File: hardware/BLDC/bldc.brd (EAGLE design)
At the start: 51 x 40 mm, 78 parts, among them J1 PWR_2_XT30PW-M, J2 LINEAR_3_JST_PH_RA, J3 LINEAR_8_JST_PH_RA, U1 MA702, U10 MCP2542FD, U11 LDFM33PUR, U2 DRV8323RS, U3 TPN7R006PL, U4 TPN7R006PL, U5 TPN7R006PL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

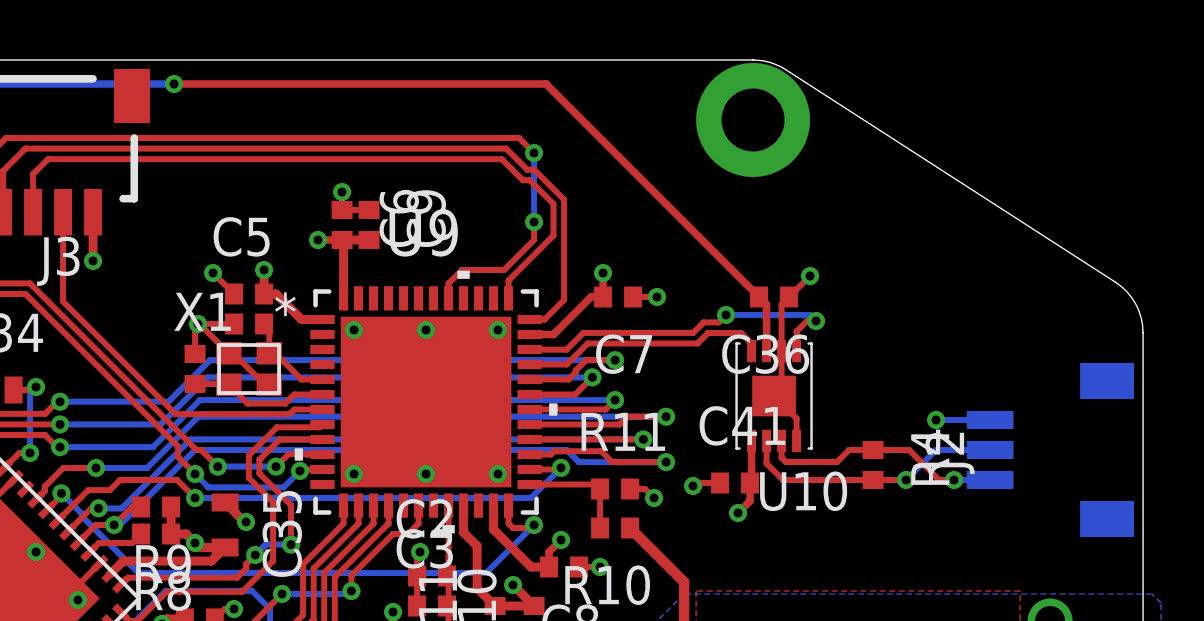
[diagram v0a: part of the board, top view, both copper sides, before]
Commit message: Added status LEDs
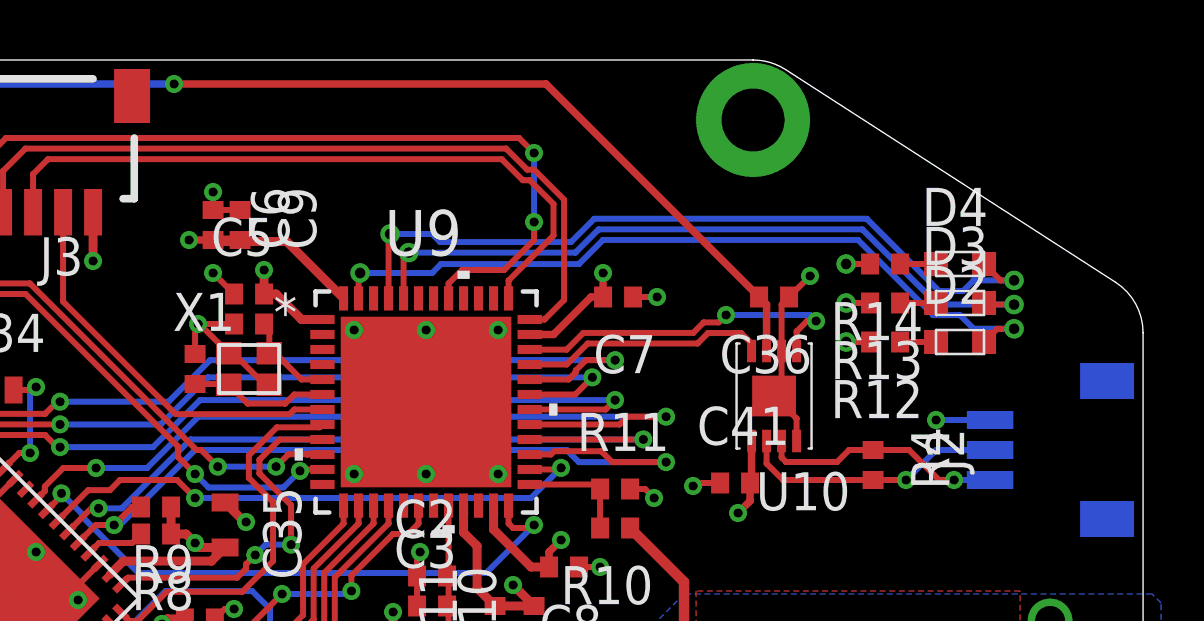
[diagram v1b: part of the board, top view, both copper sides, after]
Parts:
- added D2: 150060GS75000, _T_rcl:D0603
- added D3: 150060RS75000, _T_rcl:D0603
- added D4: 150060BS75000, _T_rcl:D0603
- added R12, R14: 5, _T_rcl:R0402
- added R13: 65, _T_rcl:R0402
- moved C6 4.30 mm to (20.0, 34.5)
- moved C9 4.30 mm to (20.9, 34.5)
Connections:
- new net N$10: D2.1, R12.2
- new net N$4: D4.1, R14.2
- new net N$7: D3.1, R13.2
- net GND: now also R12.1, R13.1, R14.1
- net LED1: now also D2.2
- net LED2: now also D3.2
- net LED3: now also D4.2
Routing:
- net LED3: track 0.00 -> 25.8 mm, vias 0 -> 2
- net LED1: track 0.00 -> 25.5 mm, vias 0 -> 2
- net LED2: track 0.00 -> 24.2 mm, vias 0 -> 2
- net +3V3: track 40.1 -> 43.3 mm
- net GND: track 58.4 -> 60.8 mm, vias 121 -> 124
- net N$7: track 0.00 -> 1.20 mm
- net N$4: track 0.00 -> 1.20 mm
- net N$10: track 0.00 -> 1.20 mm

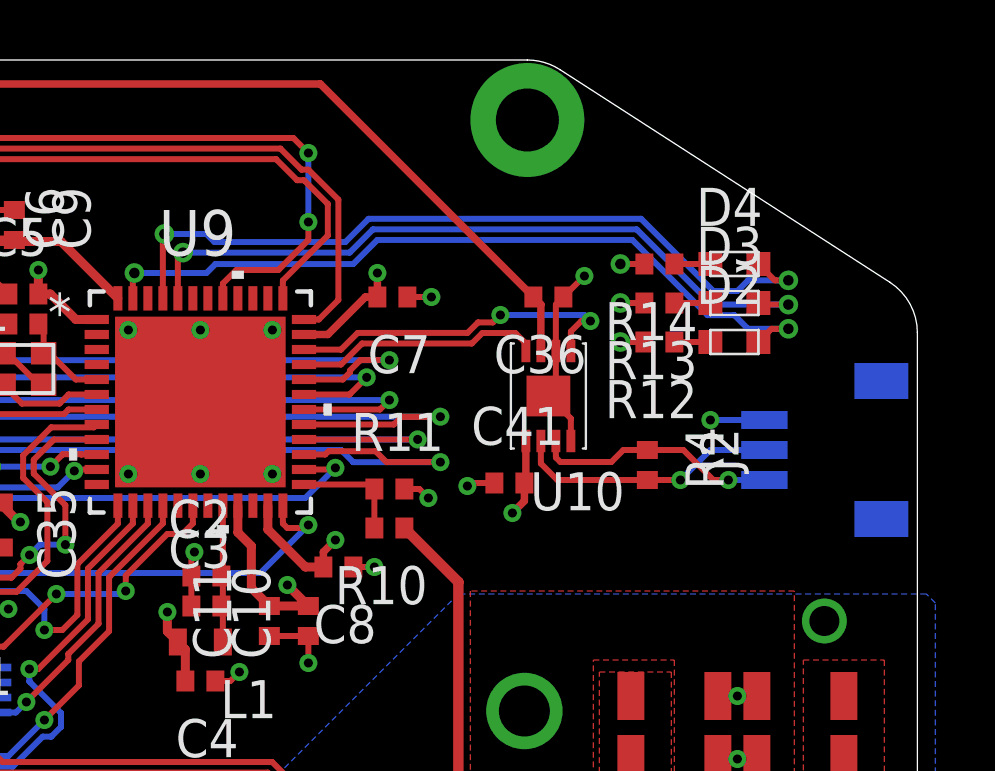
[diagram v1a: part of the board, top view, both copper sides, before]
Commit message: Moved LEDs
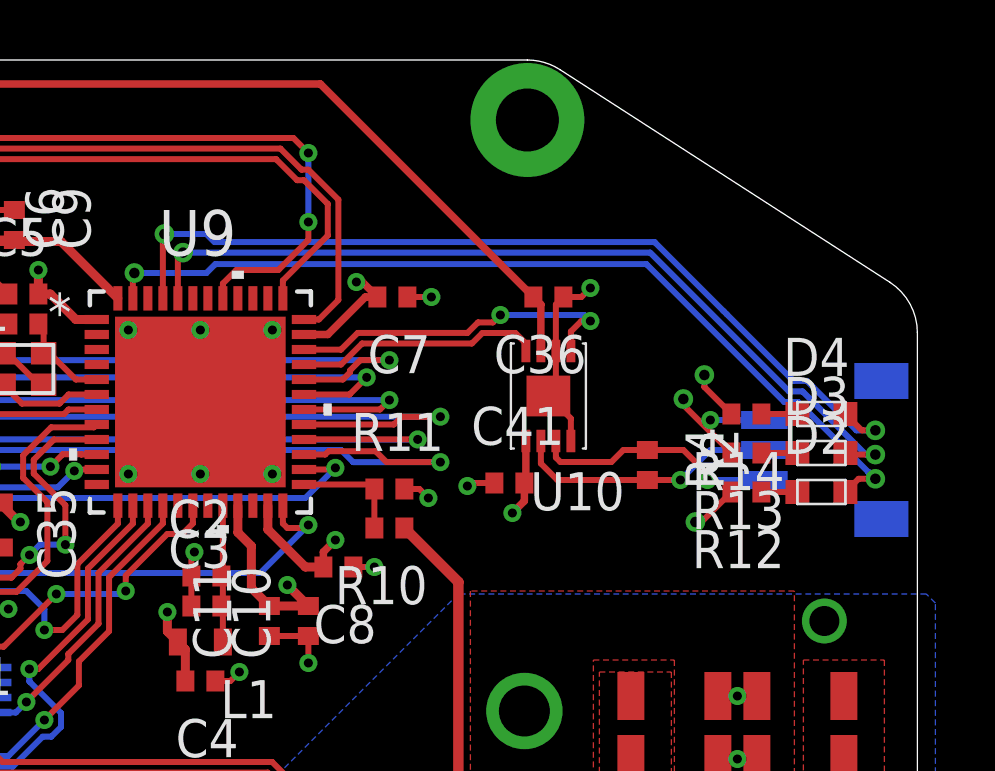
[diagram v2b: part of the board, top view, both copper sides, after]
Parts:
- moved D4 5.78 mm to (47.8, 28.2)
- moved R14 5.78 mm to (45.3, 28.2)
- moved D2 5.78 mm to (47.8, 25.6)
- moved D3 5.78 mm to (47.8, 26.9)
- moved R12 5.78 mm to (45.3, 25.6)
- moved R13 5.78 mm to (45.3, 26.9)
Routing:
- net LED2: track 24.2 -> 28.5 mm
- net LED1: track 25.5 -> 29.8 mm
- net LED3: track 25.8 -> 29.8 mm
- net GND: track 60.8 -> 64.1 mm

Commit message: Prerotate
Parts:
- moved C1 2.33 mm to (20.7, 19.4), turned to 270 degrees
- moved U1 1.41 mm to (20.0, 20.0)
- moved C10 1.03 mm to (31.6, 20.8)
- moved C4 1.00 mm to (27.1, 18.3)
- moved R9 0.71 mm to (17.6, 25.6)
- moved C9 0.70 mm to (21.6, 34.5)
- moved R10 0.63 mm to (34.0, 24.2)
- moved L1 0.60 mm to (27.1, 20.0)
- moved C8 0.58 mm to (32.2, 22.8)
- moved C11 0.51 mm to (29.5, 20.8)
- moved C25 0.41 mm to (7.00, 10.0)
- moved C28 0.41 mm to (5.20, 10.0)
- moved C27 0.41 mm to (3.40, 10.0)
- moved U3 0.41 mm to (6.10, 5.72)
- moved C3 0.30 mm to (27.3, 21.5)
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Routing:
- net +3V3: track 43.4 -> 58.6 mm
- net SHA: track 14.2 -> 25.6 mm, vias 28 -> 30
- net ENC_SCK: track 13.7 -> 10.5 mm
- net GND: track 64.1 -> 66.7 mm, vias 124 -> 123
- net ENC_CS: track 12.1 -> 10.3 mm
- net ENC_MISO: track 14.5 -> 12.8 mm
- net ENC_MOSI: track 9.22 -> 7.80 mm
- net +24V: track 40.2 -> 39.5 mm
- net N$1: track 4.66 -> 5.26 mm

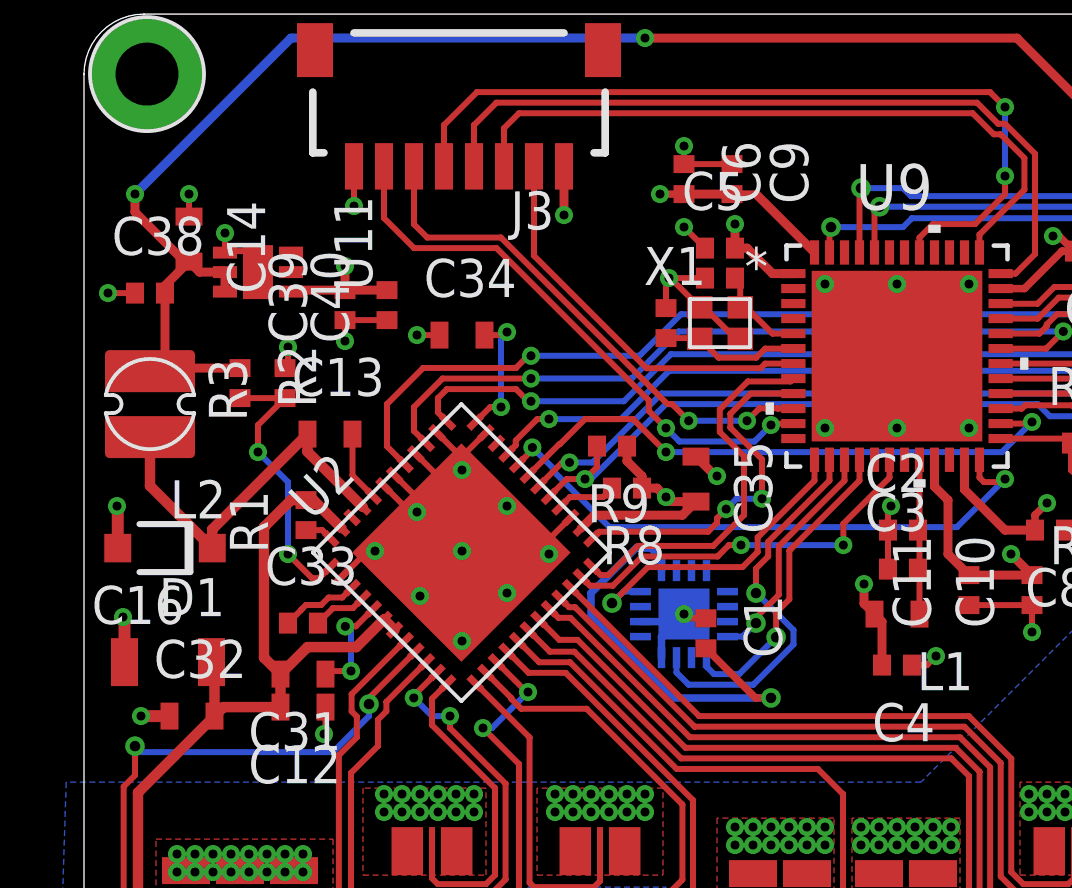
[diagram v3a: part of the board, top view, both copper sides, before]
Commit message: Fixed offset encoder
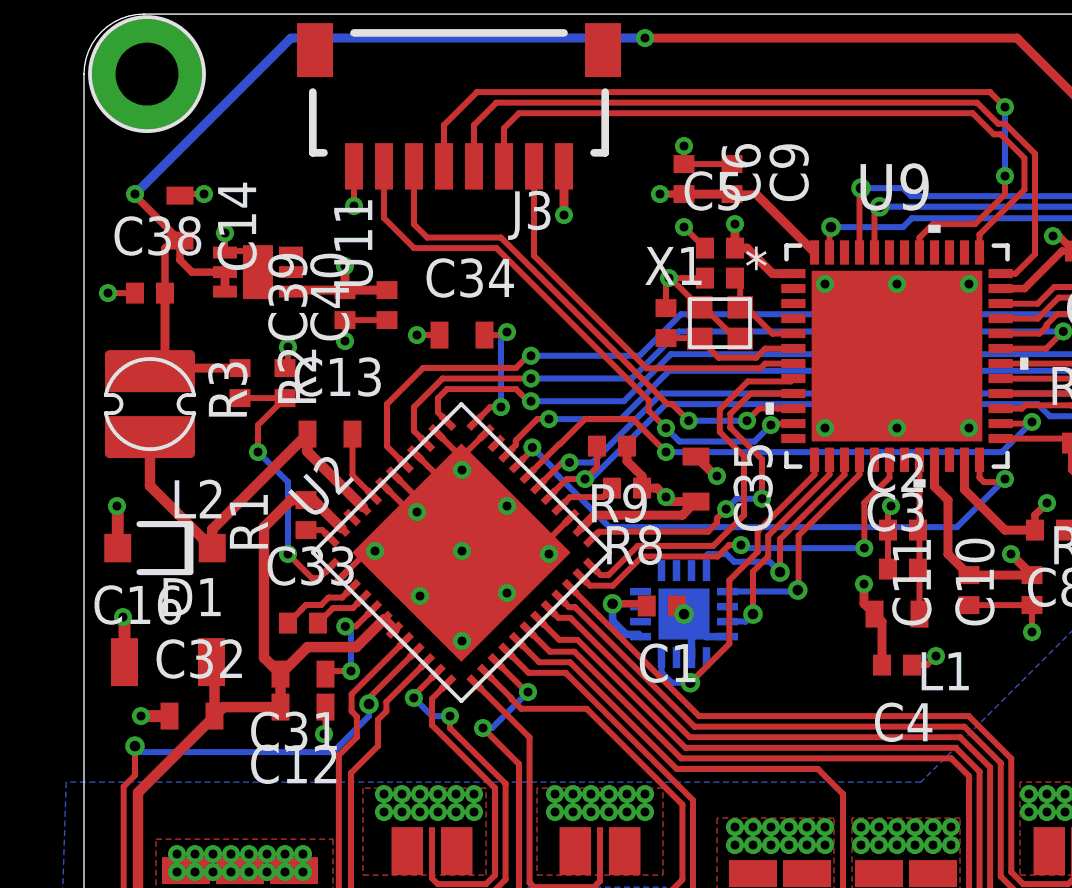
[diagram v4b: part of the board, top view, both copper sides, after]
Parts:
- moved C1 1.73 mm to (19.3, 20.3), turned to 180 degrees
- moved C14 0.76 mm to (3.20, 33.2)
- turned U1 to 270 degrees
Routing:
- net +3V3: track 58.6 -> 47.2 mm
- net ENC_MISO: track 12.8 -> 7.16 mm
- net ENC_CS: track 10.3 -> 7.56 mm
- net +5V: track 55.9 -> 56.7 mm
- net SENSE_C: track 12.9 -> 13.5 mm

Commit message: Prior to BOM consolidation
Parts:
- moved H1 0.10 mm to (2.00, 2.00)
- moved H2 0.10 mm to (2.00, 38.0)
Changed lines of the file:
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@@
 <layer number="1" name="Top" color="4" fill="1" visible="yes" active="yes"/>
 <layer number="2" name="Route2" color="16" fill="1" visible="yes" active="yes"/>
-<layer number="15" name="Route15" color="23" fill="1" visible="no" active="yes"/>
+<layer number="15" name="Route15" color="23" fill="1" visible="yes" active="yes"/>
 <layer number="16" name="Bottom" color="1" fill="1" visible="yes" active="yes"/>
 <layer number="17" name="Pads" color="2" fill="1" visible="yes" active="yes"/>
@@
 </layers>
 <board>
-<fusionsync huburn="a.YnVzaW5lc3M6Z21haWwyMjE5MTc" projecturn="a.YnVzaW5lc3M6Z21haWwyMjE5MTcjMjAxOTA2MjkyMDE0MTU5NzY" f3durn="urn:adsk.wipprod:dm.lineage:e4urj2y-ReajaBtUk_DaUw" pcbguid="" lastpulledtime="" lastsyncedchangeguid="" latestrevisionid="c8898aa8-4816-4024-a727-549153469479" lastsyncedrevisionid="c8898aa8-4816-4024-a727-549153469479" lastboardhashguid="96ba5604-6864-0f3b-cda7-083015d9c990" lastpushedtime="2020-05-19T04:17:52Z" linktopcb3d="%12"/>
+<fusionsync huburn="a.YnVzaW5lc3M6Z21haWwyMjE5MTc" projecturn="a.YnVzaW5lc3M6Z21haWwyMjE5MTcjMjAxOTA2MjkyMDE0MTU5NzY" f3durn="urn:adsk.wipprod:dm.lineage:e4urj2y-ReajaBtUk_DaUw" pcbguid="" lastpulledtime="" lastsyncedchangeguid="" latestrevisionid="0cfa6979-0abf-47e5-904f-7e41c382e9f9" lastsyncedrevisionid="0cfa6979-0abf-47e5-904f-7e41c382e9f9" lastboardhashguid="129d7aed-9189-2586-7fe0-9e496c46e9fb" lastpushedtime="2020-05-19T04:37:09Z" linktopcb3d="%12"/>
 <plain>
 <wire x1="39.0836" y1="39.681" x2="38" y2="40" width="0" layer="20" curve="32.8049"/>
@@
 <attribute name="VALUE" x="36.65" y="8.95" size="1.27" layer="27" rot="R180"/>
 </element>
-<element name="H1" library="_T_conn" library_urn="urn:adsk.eagle:library:19570503" package="M2" package3d_urn="urn:adsk.eagle:package:20293119/4" value="PCB_MOUNT_HOLE_M2" x="2.1" y="2" smashed="yes"/>
-<element name="H2" library="_T_conn" library_urn="urn:adsk.eagle:library:19570503" package="M2" package3d_urn="urn:adsk.eagle:package:20293119/4" value="PCB_MOUNT_HOLE_M2" x="2.1" y="38" smashed="yes"/>
+<element name="H1" library="_T_conn" library_urn="urn:adsk.eagle:library:19570503" package="M2" package3d_urn="urn:adsk.eagle:package:20293119/4" value="PCB_MOUNT_HOLE_M2" x="2" y="2" smashed="yes"/>
+<element name="H2" library="_T_conn" library_urn="urn:adsk.eagle:library:19570503" package="M2" package3d_urn="urn:adsk.eagle:package:20293119/4" value="PCB_MOUNT_HOLE_M2" x="2" y="38" smashed="yes"/>
 <element name="H3" library="_T_conn" library_urn="urn:adsk.eagle:library:19570503" package="M2" package3d_urn="urn:adsk.eagle:package:20293119/4" value="PCB_MOUNT_HOLE_M2" x="38" y="2" smashed="yes"/>
 <element name="H4" library="_T_conn" library_urn="urn:adsk.eagle:library:19570503" package="M2" package3d_urn="urn:adsk.eagle:package:20293119/4" value="PCB_MOUNT_HOLE_M2" x="38" y="38" smashed="yes"/>

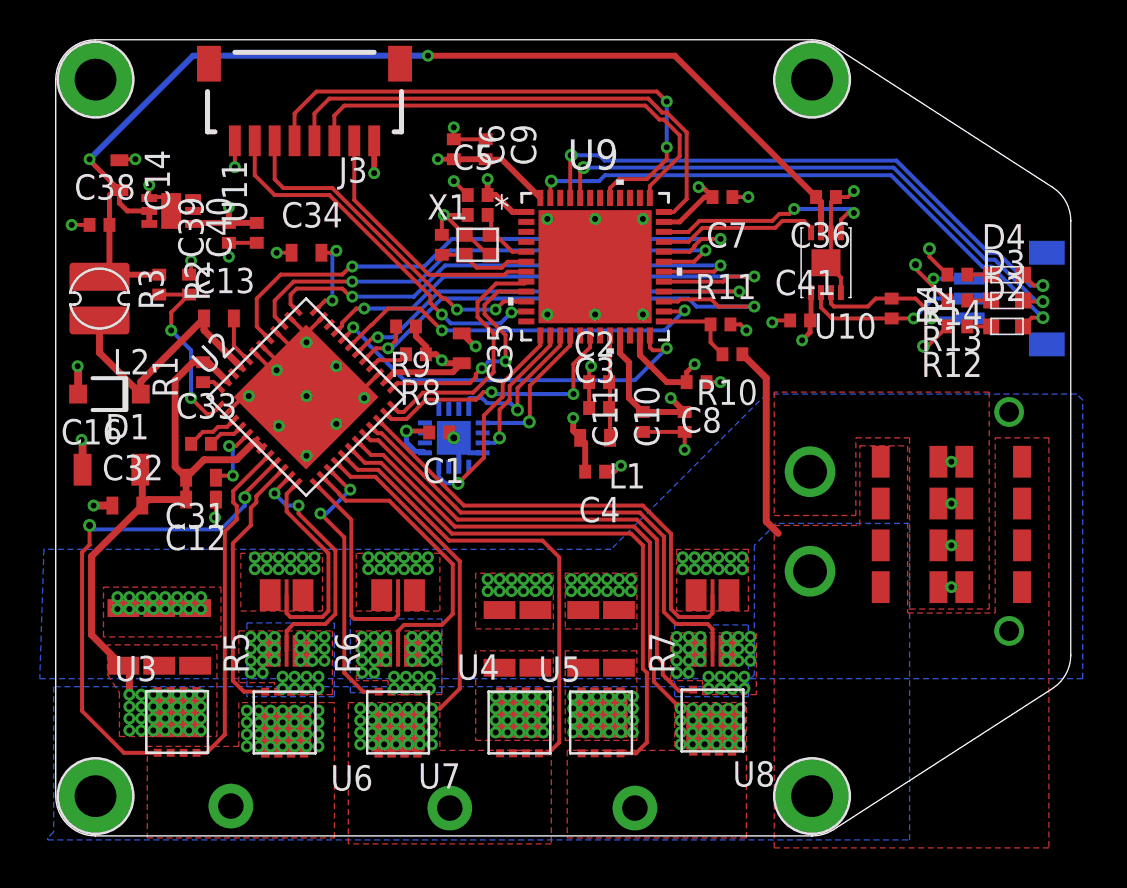
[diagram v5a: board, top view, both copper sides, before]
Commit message: BoM consolidation and package standardization
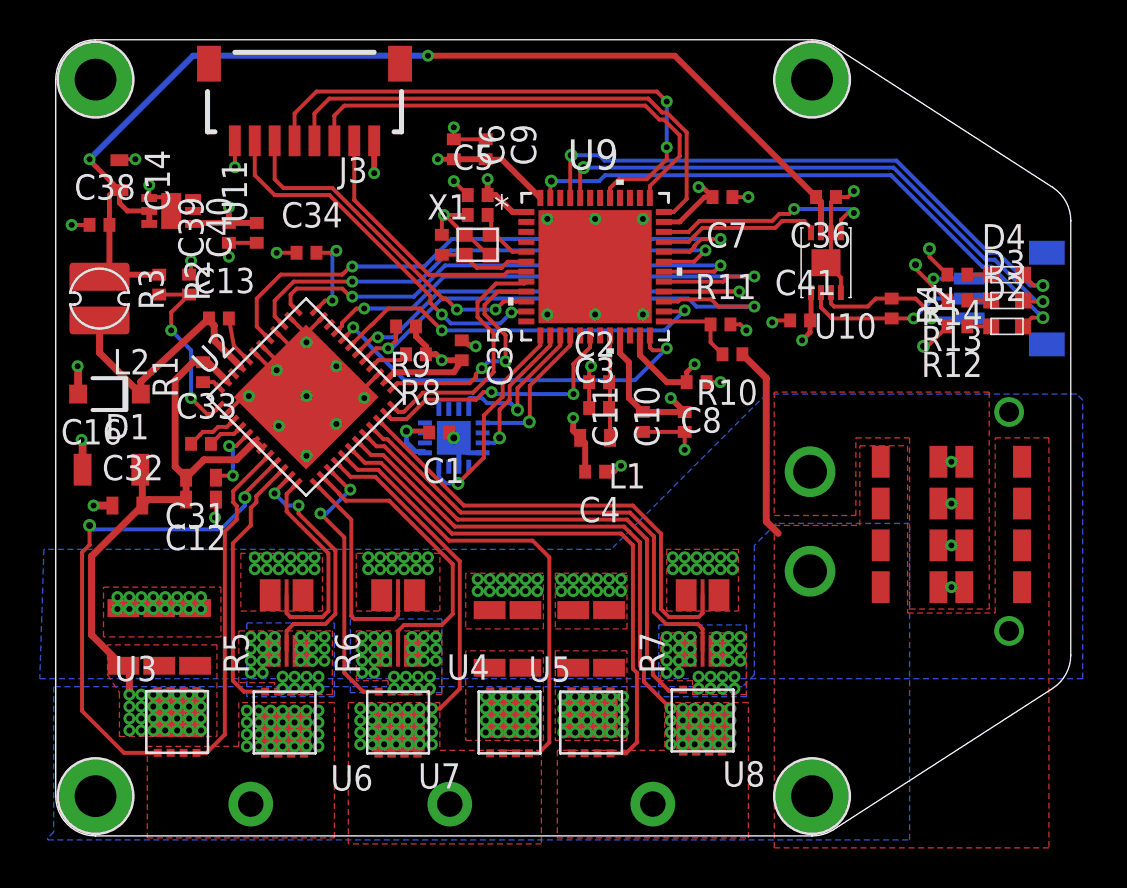
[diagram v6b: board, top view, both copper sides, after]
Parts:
- C13, C34, C35: device _T_rcl:C0603 -> _T_rcl:C0402
- C14: value 2.2uF 10V -> 2.2uF 50V
- C36, C41: value 0.1uF 10V -> 100nF 10V
- moved PHASE_A 1.00 mm to (9.80, 1.60)
- moved PHASE_C 0.92 mm to (30.0, 1.60)
- moved C24 0.50 mm to (26.0, 9.90)
- moved C26 0.50 mm to (27.8, 9.90)
- moved C29 0.50 mm to (23.6, 9.90)
- moved GND 0.50 mm to (21.8, 9.90)
- moved R7 0.50 mm to (32.5, 10.7)
- moved U4 0.50 mm to (22.8, 5.70)
- moved U5 0.50 mm to (26.9, 5.70)
- moved U8 0.50 mm to (32.5, 5.80)
- moved PHASE_B 0.20 mm to (19.8, 1.60)
- moved C35 0.10 mm to (20.4, 24.4)
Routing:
- net SPC: track 24.6 -> 24.1 mm
- net SNC: track 24.1 -> 23.6 mm
- net SHC: track 25.8 -> 25.3 mm
- net GLC: track 25.7 -> 25.2 mm
- net GHC: track 28.2 -> 27.7 mm
- net GHB: track 23.5 -> 23.0 mm
